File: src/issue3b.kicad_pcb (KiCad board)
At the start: 2 copper layers, 213.1 x 129 mm, 126 parts, among them T1 Coil, X1 14Mhz, X2 4.43Mhz

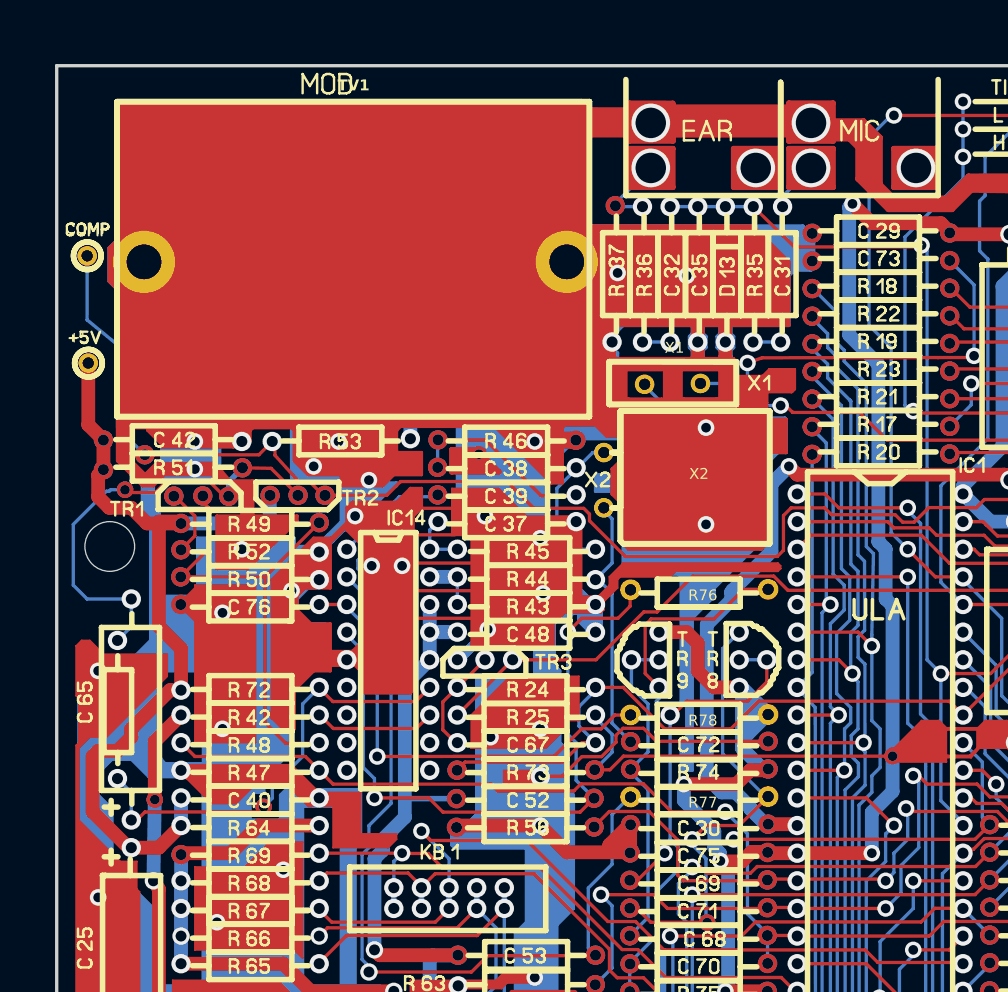
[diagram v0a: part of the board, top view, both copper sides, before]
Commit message: changed to kicad 10 and added bljall-alt 3d models.
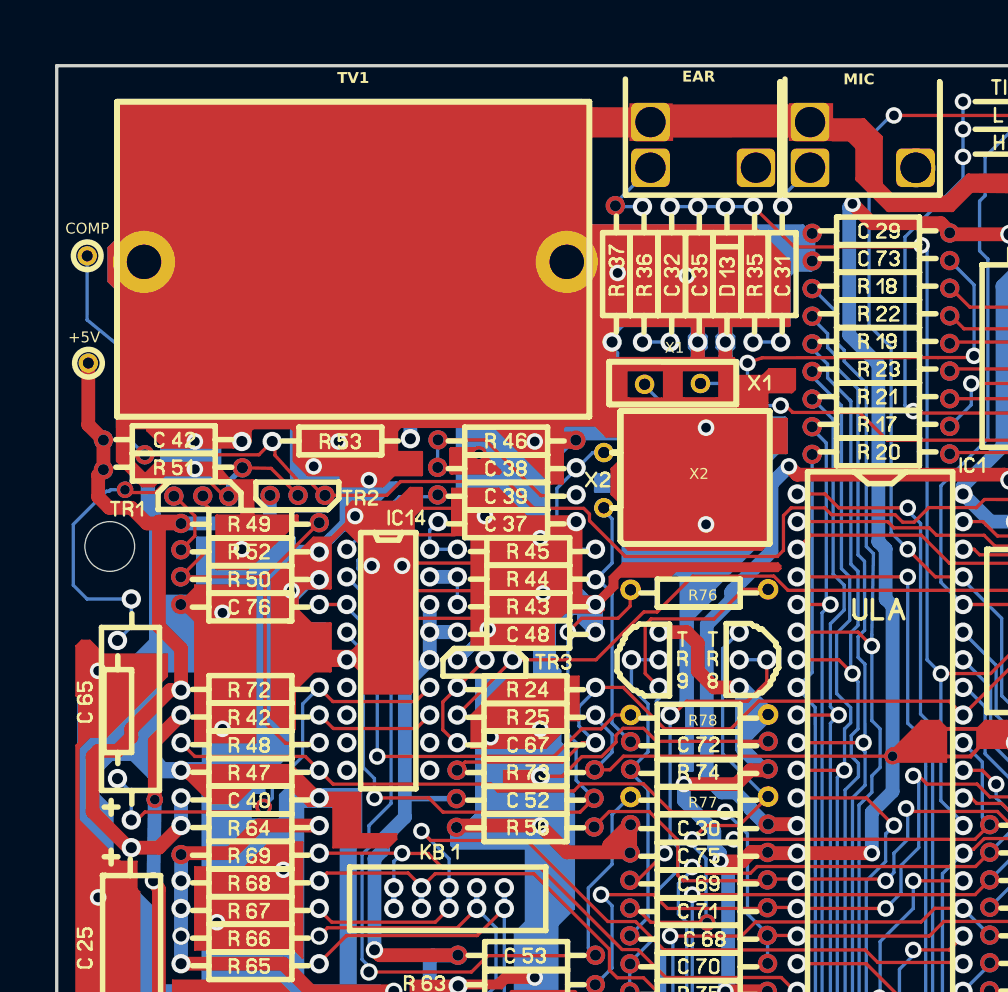
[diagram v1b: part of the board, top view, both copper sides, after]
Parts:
- added EAR: Barrel_Jack, spectrum3b:Audio-Connector, F.Cu at (102.0, 26.5)
- added MIC: Barrel_Jack, spectrum3b:Audio-Connector, F.Cu at (116.7, 26.5)
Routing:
- net (no net): track 14494.9 -> 14361.0 mm, vias 833 -> 827
- net GND: track 5520.4 -> 5465.5 mm, vias 179 -> 175
- net Net-(EAR1-Pad2): track 0.00 -> 7.35 mm, vias 0 -> 2
- net Net-(C31-Pad2): track 0.00 -> 4.64 mm, vias 0 -> 1
- net VIDEO: vias 7 -> 6
- net Net-(TR2-C): vias 9 -> 8
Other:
- board text removed: "COMP"
